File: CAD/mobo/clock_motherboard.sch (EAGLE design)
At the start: 32 parts, among them IC1 LM1086CT-5.0, IC2 LM1086CT-3.3, J2 2.1MMJACK, U1 ATMEGA328P_PDIP, U2 DS1307, Y2 32.768

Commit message: Updating motherboard CAD files (OSHpark version)
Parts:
- added GND: (no value), SparkFun-Connectors:M06NO_SILK_FEMALE_PTH
- added RDIV: 10K, rcl-ez:R-US_0207/5V
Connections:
- net A0: now also RDIV.2
- net GND: now also GND.1, GND.2, GND.3, GND.4, GND.5, GND.6, JP4.3; no longer JP4.1
- net VCC: now also RDIV.1
- net VIN: now also JP4.1; no longer JP4.3
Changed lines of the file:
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@@
 <part name="P+7" library="supply1" deviceset="VCC" device=""/>
 <part name="GND12" library="supply1" deviceset="GND" device=""/>
+<part name="RDIV" library="rcl-ez" deviceset="R-US_" device="0207/5V" value="10K"/>
+<part name="P+8" library="supply1" deviceset="VCC" device=""/>
+<part name="GND" library="SparkFun-Connectors" deviceset="M06" device="NO_SILK_FEMALE_PTH"/>
+<part name="GND13" library="supply1" deviceset="GND" device=""/>
 </parts>
 <sheets>
@@
 <attribute name="VALUE" x="213.36" y="43.18" size="1.778" layer="96" rot="MR180"/>
 </instance>
-<instance part="GND12" gate="1" x="215.9" y="25.4" smashed="yes">
-<attribute name="VALUE" x="213.36" y="22.86" size="1.778" layer="96"/>
+<instance part="GND12" gate="1" x="208.28" y="30.48" smashed="yes">
+<attribute name="VALUE" x="205.74" y="27.94" size="1.778" layer="96"/>
+</instance>
+<instance part="RDIV" gate="G$1" x="231.14" y="134.62" rot="MR270"/>
+<instance part="P+8" gate="VCC" x="231.14" y="144.78" smashed="yes" rot="MR0">
+<attribute name="VALUE" x="228.6" y="147.32" size="1.778" layer="96" rot="MR180"/>
+</instance>
+<instance part="GND" gate="G$1" x="198.12" y="149.86"/>
+<instance part="GND13" gate="1" x="205.74" y="139.7" smashed="yes">
+<attribute name="VALUE" x="203.2" y="137.16" size="1.778" layer="96"/>
 </instance>
 </instances>
@@
 <segment>
 <pinref part="GND12" gate="1" pin="GND"/>
-<wire x1="215.9" y1="27.94" x2="215.9" y2="30.48" width="0.1524" layer="91"/>
-<pinref part="JP4" gate="G$1" pin="1"/>
-<wire x1="215.9" y1="30.48" x2="220.98" y2="30.48" width="0.1524" layer="91"/>
+<wire x1="208.28" y1="33.02" x2="208.28" y2="35.56" width="0.1524" layer="91"/>
+<pinref part="JP4" gate="G$1" pin="3"/>
+<wire x1="208.28" y1="35.56" x2="220.98" y2="35.56" width="0.1524" layer="91"/>
+</segment>
+<segment>
+<pinref part="GND" gate="G$1" pin="1"/>
+<pinref part="GND13" gate="1" pin="GND"/>
+<wire x1="203.2" y1="144.78" x2="205.74" y2="144.78" width="0.1524" layer="91"/>
+<wire x1="205.74" y1="142.24" x2="205.74" y2="144.78" width="0.1524" layer="91"/>
+<pinref part="GND" gate="G$1" pin="6"/>
+<wire x1="205.74" y1="144.78" x2="205.74" y2="147.32" width="0.1524" layer="91"/>
+<wire x1="205.74" y1="147.32" x2="205.74" y2="149.86" width="0.1524" layer="91"/>
+<wire x1="205.74" y1="149.86" x2="205.74" y2="152.4" width="0.1524" layer="91"/>
+<wire x1="205.74" y1="152.4" x2="205.74" y2="154.94" width="0.1524" layer="91"/>
+<wire x1="205.74" y1="154.94" x2="205.74" y2="157.48" width="0.1524" layer="91"/>
+<wire x1="205.74" y1="157.48" x2="203.2" y2="157.48" width="0.1524" layer="91"/>
+<pinref part="GND" gate="G$1" pin="5"/>
+<wire x1="203.2" y1="154.94" x2="205.74" y2="154.94" width="0.1524" layer="91"/>
+<pinref part="GND" gate="G$1" pin="4"/>
+<wire x1="203.2" y1="152.4" x2="205.74" y2="152.4" width="0.1524" layer="91"/>
+<pinref part="GND" gate="G$1" pin="3"/>
+<wire x1="203.2" y1="149.86" x2="205.74" y2="149.86" width="0.1524" layer="91"/>
+<pinref part="GND" gate="G$1" pin="2"/>
+<wire x1="203.2" y1="147.32" x2="205.74" y2="147.32" width="0.1524" layer="91"/>
+<junction x="205.74" y="154.94"/>
+<junction x="205.74" y="152.4"/>
+<junction x="205.74" y="149.86"/>
+<junction x="205.74" y="147.32"/>
+<junction x="205.74" y="144.78"/>
 </segment>
 </net>
@@
 <wire x1="215.9" y1="38.1" x2="215.9" y2="33.02" width="0.1524" layer="91"/>
 </segment>
+<segment>
+<pinref part="P+8" gate="VCC" pin="VCC"/>
+<pinref part="RDIV" gate="G$1" pin="1"/>
+<wire x1="231.14" y1="142.24" x2="231.14" y2="139.7" width="0.1524" layer="91"/>
+</segment>
 </net>
 <net name="N$14" class="0">
@@
 <pinref part="U1" gate="G$1" pin="PC0(ADC0)"/>
 <label x="203.2" y="127" size="1.778" layer="95"/>
-<wire x1="264.16" y1="127" x2="200.66" y2="127" width="0.1524" layer="91"/>
+<wire x1="264.16" y1="127" x2="231.14" y2="127" width="0.1524" layer="91"/>
 <pinref part="JP1" gate="G$1" pin="A0"/>
+<pinref part="RDIV" gate="G$1" pin="2"/>
+<wire x1="231.14" y1="127" x2="200.66" y2="127" width="0.1524" layer="91"/>
+<wire x1="231.14" y1="129.54" x2="231.14" y2="127" width="0.1524" layer="91"/>
+<junction x="231.14" y="127"/>
 </segment>
 </net>
@@
 <net name="VIN" class="0">
 <segment>
-<pinref part="JP4" gate="G$1" pin="3"/>
-<wire x1="220.98" y1="35.56" x2="205.74" y2="35.56" width="0.1524" layer="91"/>
-<label x="205.74" y="35.56" size="1.778" layer="95"/>
-</segment>
-<segment>
 <wire x1="264.16" y1="104.14" x2="251.46" y2="104.14" width="0.1524" layer="91"/>
 <label x="254" y="104.14" size="1.778" layer="95"/>
@@
 <label x="116.84" y="45.72" size="1.778" layer="95"/>
 </segment>
-</net>
+<segment>
+<pinref part="JP4" gate="G$1" pin="1"/>
+<wire x1="220.98" y1="30.48" x2="213.36" y2="30.48" width="0.1524" layer="91"/>
+<label x="213.36" y="30.48" size="1.778" layer="95"/>
+</segment>
+</net>

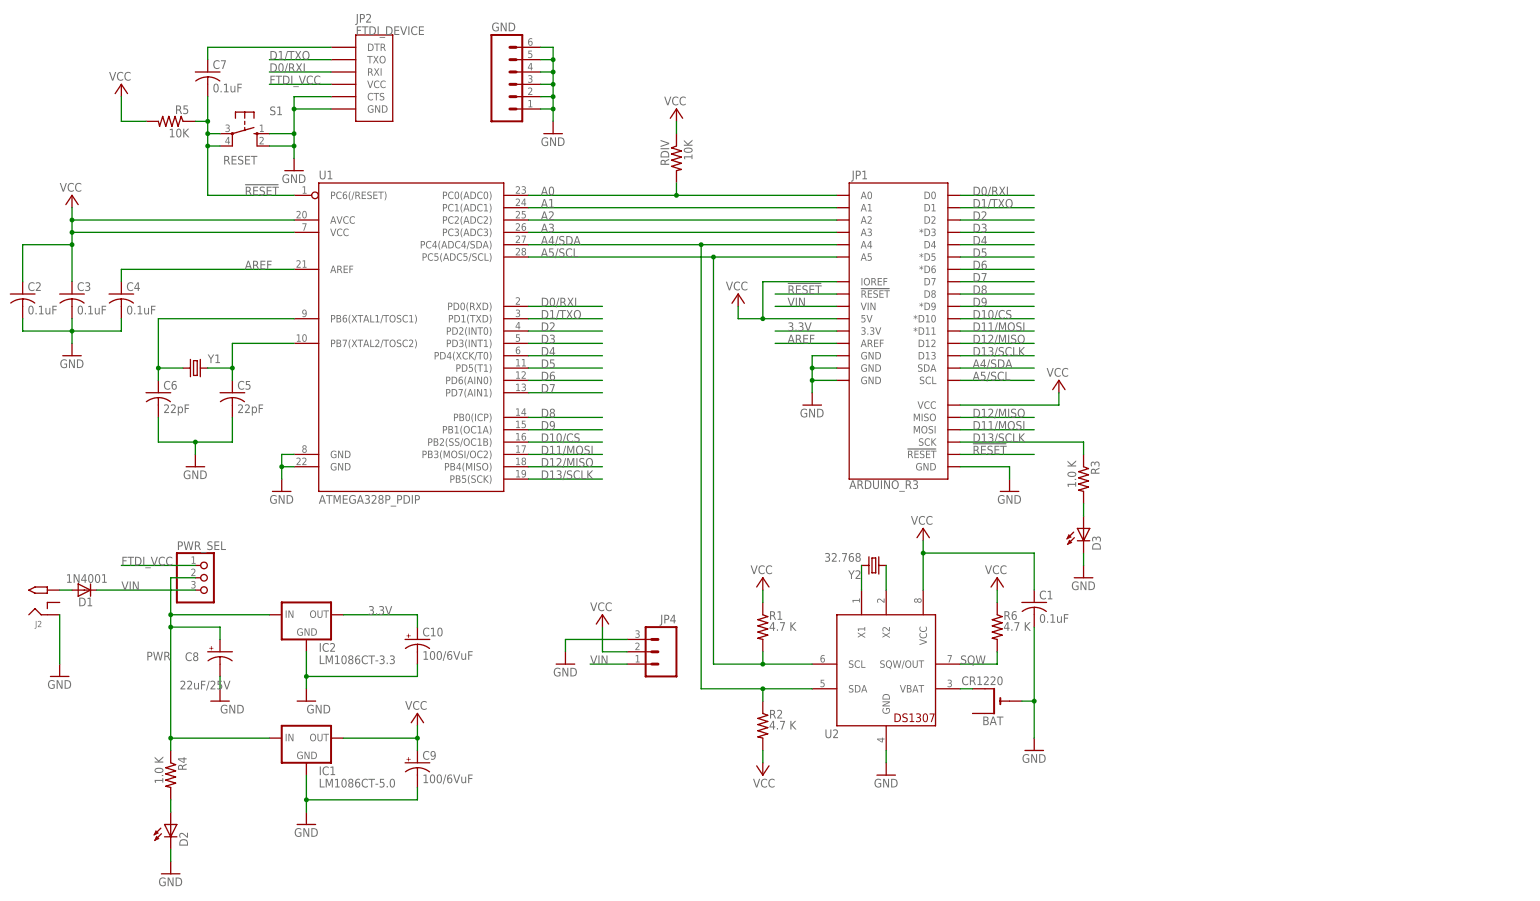
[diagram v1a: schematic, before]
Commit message: Adding updated part database and motherboard BOM, closes #4
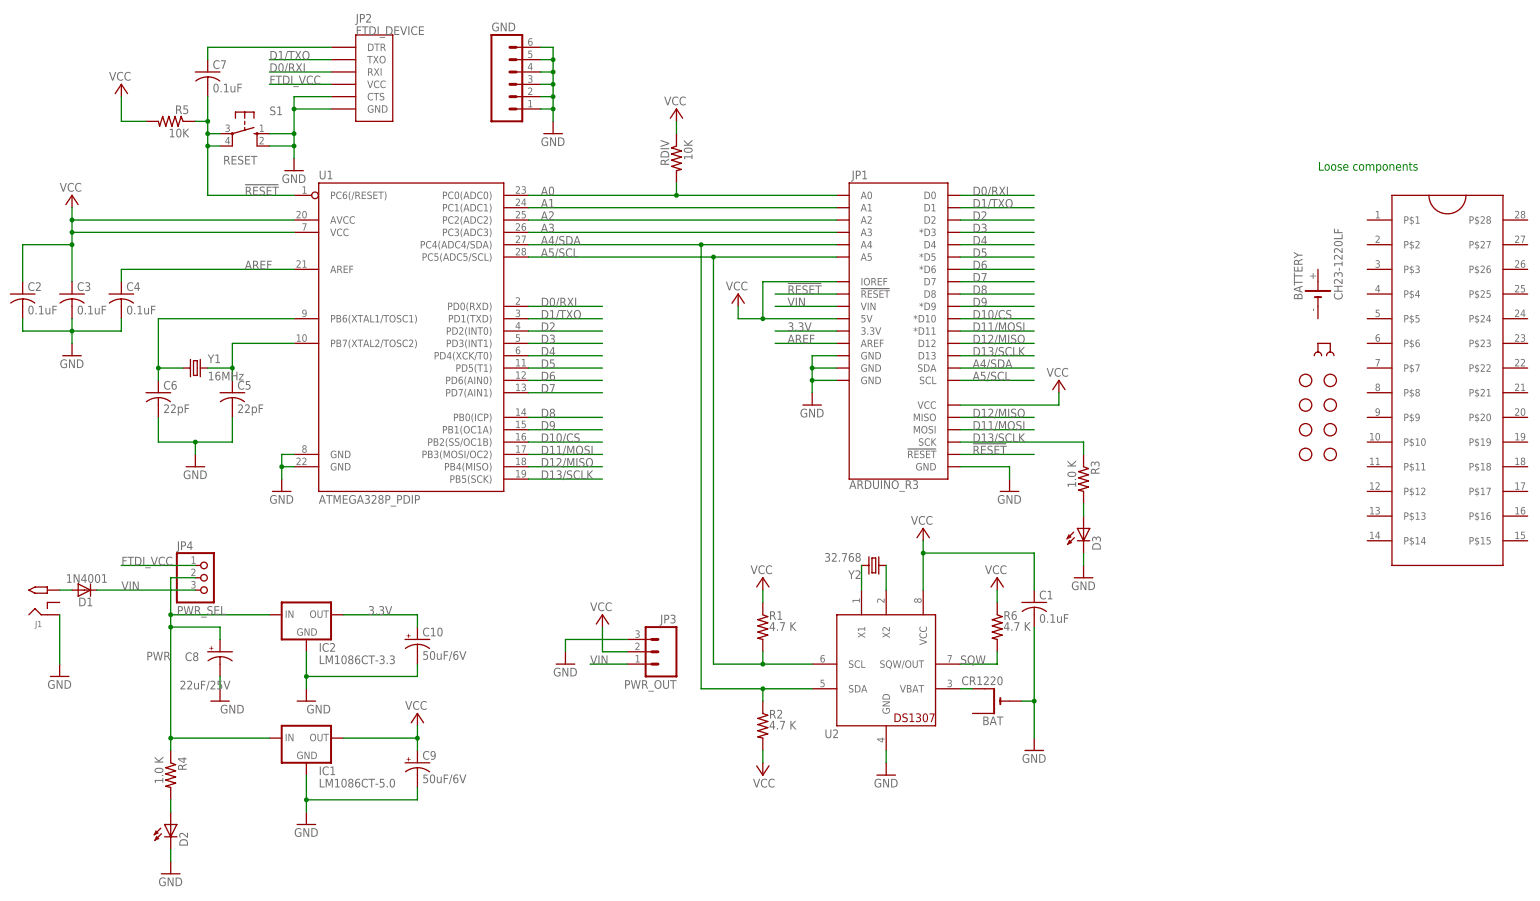
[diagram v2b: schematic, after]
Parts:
- removed PWR_SEL: (no value), pinhead:PINHD-1X3
- added BATTERY: CH23-1220LF, battery:CH23-1220LF
- added J1: 2.1MMJACK, minimidi:2.1MMJACK
- added JP3: PWR_OUT, SparkFun-Connectors:M03SCREW
- added SOCKET: ZIFSOCKET-28-3ZIFFSOCKET-28-3, SparkFun-Connectors:ZIFSOCKET-28-3ZIFFSOCKET-28-3
- added STANDOFF1, STANDOFF2, STANDOFF3, STANDOFF4, STANDOFF5, STANDOFF6, STANDOFF7, STANDOFF8: STAND-OFF, SparkFun-Electromechanical:STAND-OFF
- BAT: PARTNO (none) -> 3001
- C1, C2, C3, C4, C7: PARTNO (none) -> 21RZ310-RC
- C10, C9: value 100/6VuF -> 50uF/6V; PARTNO (none) -> ECA-1CM470I
- C5, C6: PARTNO (none) -> K220J15C0GF5TL2
- C8: PARTNO (none) -> EEU-FR1H220B
- D1: PARTNO (none) -> 1N4001-TP
- D2: value (none) -> RED; PARTNO (none) -> WP7113SRD/D
- D3: value (none) -> YELLOW; PARTNO (none) -> WP7113SYD
- GND, JP1: BOM (none) -> EXCLUDE
- IC1: PARTNO (none) -> LM1086CT-5.0/NOPB
- IC2: PARTNO (none) -> LM1086CT-3.3/NOPB
- J2: value 2.1MMJACK -> PWR_SEL; device minimidi:2.1MMJACK -> jumper:JUMPER; PARTNO (none) -> 382811-8
- JP2: PARTNO (none) -> 68000-406HLF
- JP4: value (none) -> PWR_SEL; device SparkFun-Connectors:M03SCREW -> pinhead:PINHD-1X3; PARTNO (none) -> 68001-403HLF
- R1, R2, R6: PARTNO (none) -> CFR-25JB-52-4K7
- R3, R4: PARTNO (none) -> CFR-25JB-52-1K
- R5, RDIV: PARTNO (none) -> CFR-25JB-52-10K
- U1: PARTNO (none) -> ATMEGA328P-PU
- U2: PARTNO (none) -> DS1307+
- Y1: value (none) -> 16MHz; PARTNO (none) -> HC49US-16.000MABJ-UB
- Y2: PARTNO (none) -> AB38T-32.768KHZ
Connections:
- net FTDI_VCC: now also JP4.1; no longer PWR_SEL.1
- net GND: now also J1.RING, JP3.3; no longer J2.RING, JP4.3
- net N$17: now also J1.TIP; no longer J2.TIP
- net PWR: now also JP4.2; no longer PWR_SEL.2
- net VCC: now also JP3.2; no longer JP4.2
- net VIN: now also JP3.1, JP4.3; no longer JP4.1, PWR_SEL.3
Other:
- note added: "Loose components"

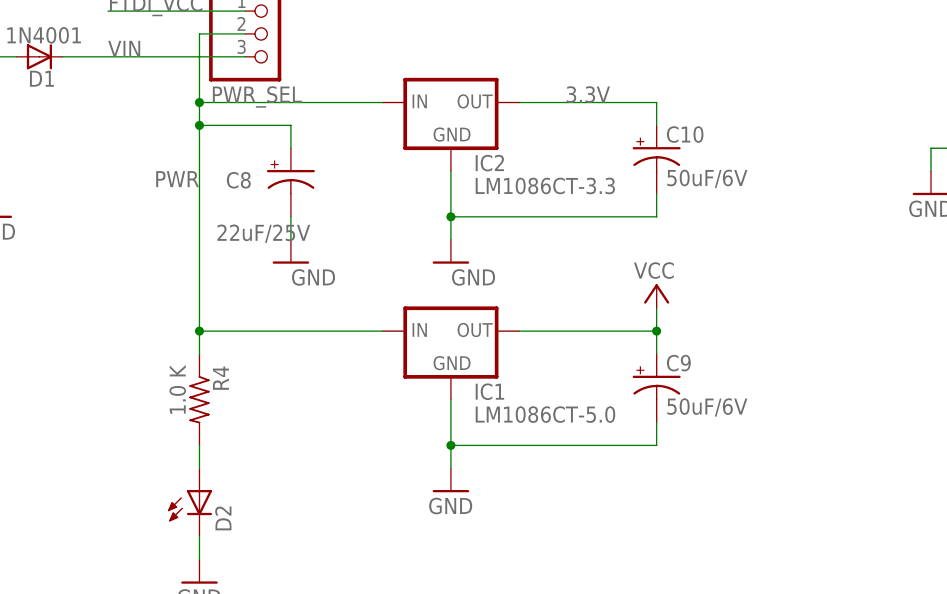
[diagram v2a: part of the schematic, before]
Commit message: Fixed mobo power circuit and updated BOM
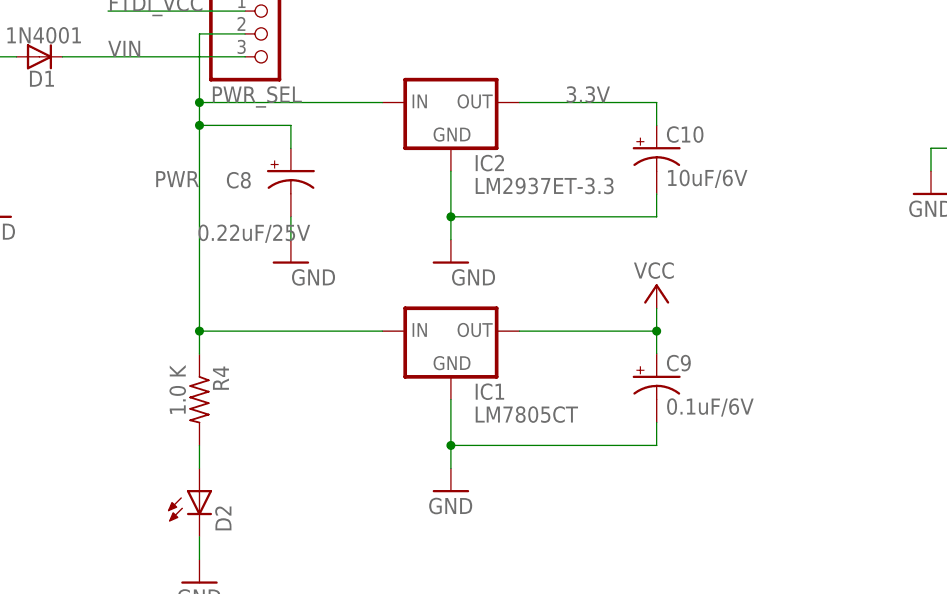
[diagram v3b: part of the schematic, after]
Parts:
- C10: value 50uF/6V -> 10uF/6V; PARTNO ECA-1CM470I -> A758BG106M1EAAE070
- C8: value 22uF/25V -> 0.22uF/25V; PARTNO EEU-FR1H220B -> FG14X7R1H224KNT06
- C9: value 50uF/6V -> 0.1uF/6V; PARTNO ECA-1CM470I -> 21RZ310-RC
- IC1: value LM1086CT-5.0 -> LM7805CT; PARTNO LM1086CT-5.0/NOPB -> LM7805CT/NOPB
- IC2: value LM1086CT-3.3 -> LM2937ET-3.3; PARTNO LM1086CT-3.3/NOPB -> LM2937ET-3.3/NOPB
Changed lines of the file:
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@@
 </part>
 <part name="S1" library="switch-omron" deviceset="10-XX" device="" value="RESET"/>
-<part name="IC2" library="v-reg" deviceset="78XXS" device="" value="LM1086CT-3.3">
-<attribute name="PARTNO" value="LM1086CT-3.3/NOPB"/>
+<part name="IC2" library="v-reg" deviceset="78XXS" device="" value="LM2937ET-3.3">
+<attribute name="PARTNO" value="LM2937ET-3.3/NOPB"/>
 </part>
-<part name="IC1" library="v-reg" deviceset="78XXS" device="" value="LM1086CT-5.0">
-<attribute name="PARTNO" value="LM1086CT-5.0/NOPB"/>
+<part name="IC1" library="v-reg" deviceset="78XXS" device="" value="LM7805CT">
+<attribute name="PARTNO" value="LM7805CT/NOPB"/>
 </part>
 <part name="J1" library="minimidi" deviceset="2.1MMJACK" device="">
@@
 <part name="GND10" library="supply1" deviceset="GND" device=""/>
 <part name="P+1" library="supply1" deviceset="VCC" device=""/>
-<part name="C10" library="minimidi" deviceset="CPOL-US" device="E2.5-6" value="50uF/6V">
-<attribute name="PARTNO" value="ECA-1CM470I"/>
+<part name="C10" library="minimidi" deviceset="CPOL-US" device="E2.5-6" value="10uF/6V">
+<attribute name="PARTNO" value="A758BG106M1EAAE070"/>
 </part>
 <part name="JP4" library="pinhead" deviceset="PINHD-1X3" device="" value="PWR_SEL">
 <attribute name="PARTNO" value="68001-403HLF"/>
 </part>
-<part name="C9" library="minimidi" deviceset="CPOL-US" device="E2.5-6" value="50uF/6V">
-<attribute name="PARTNO" value="ECA-1CM470I"/>
+<part name="C9" library="minimidi" deviceset="CPOL-US" device="E2.5-6" value="0.1uF/6V">
+<attribute name="PARTNO" value="21RZ310-RC"/>
 </part>
 <part name="R1" library="minimidi" deviceset="R-US_" device="0207/5V" value="4.7 K">
@@
 </part>
 <part name="GND7" library="supply1" deviceset="GND" device=""/>
-<part name="C8" library="minimidi" deviceset="CPOL-US" device="E2.5-6" value="22uF/25V">
-<attribute name="PARTNO" value="EEU-FR1H220B"/>
+<part name="C8" library="minimidi" deviceset="CPOL-US" device="E2.5-6" value="0.22uF/25V">
+<attribute name="PARTNO" value="FG14X7R1H224KNT06"/>
 </part>
 <part name="GND11" library="supply1" deviceset="GND" device=""/>
